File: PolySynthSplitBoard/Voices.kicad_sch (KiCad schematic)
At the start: 42 parts, among them J701 VoiceBoardConn_20P_200P, J702 VoiceBoardConn_20P_200P, J703 VoiceBoardConn_20P_200P, J704 VoiceBoardConn_20P_200P, J705 VoiceBoardConn_20P_200P, J706 VoiceBoardConn_20P_200P, U701 TCA9548APWR, U703 L7805, U704 L7905

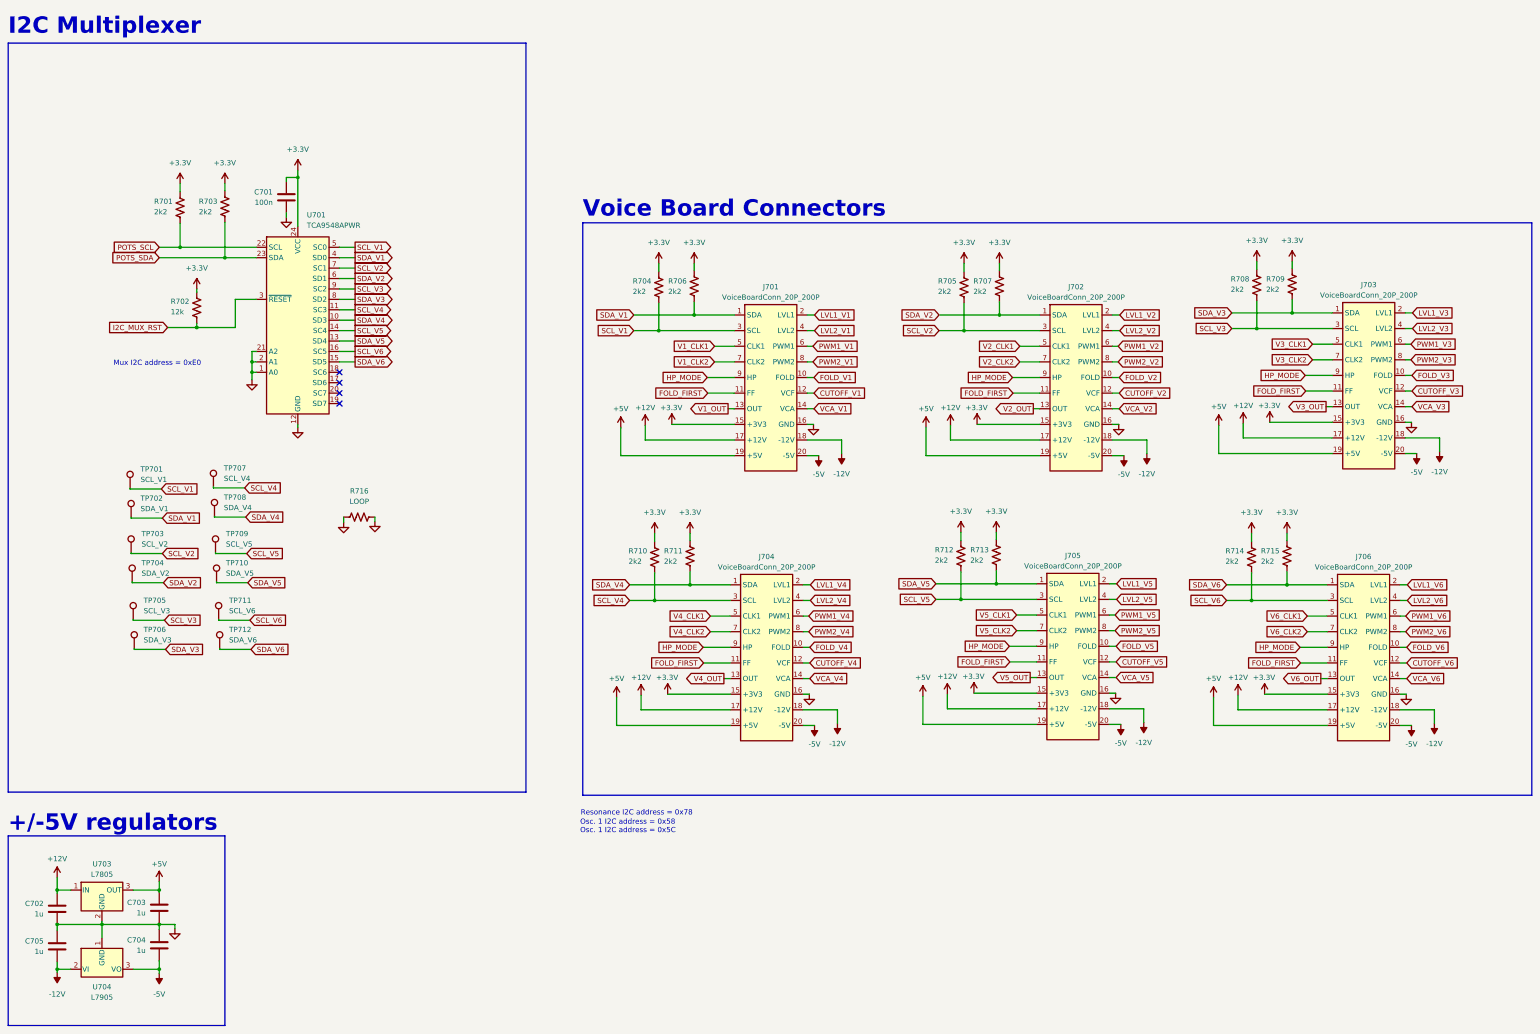
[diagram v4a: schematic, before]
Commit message: double buffering voice clock fixes
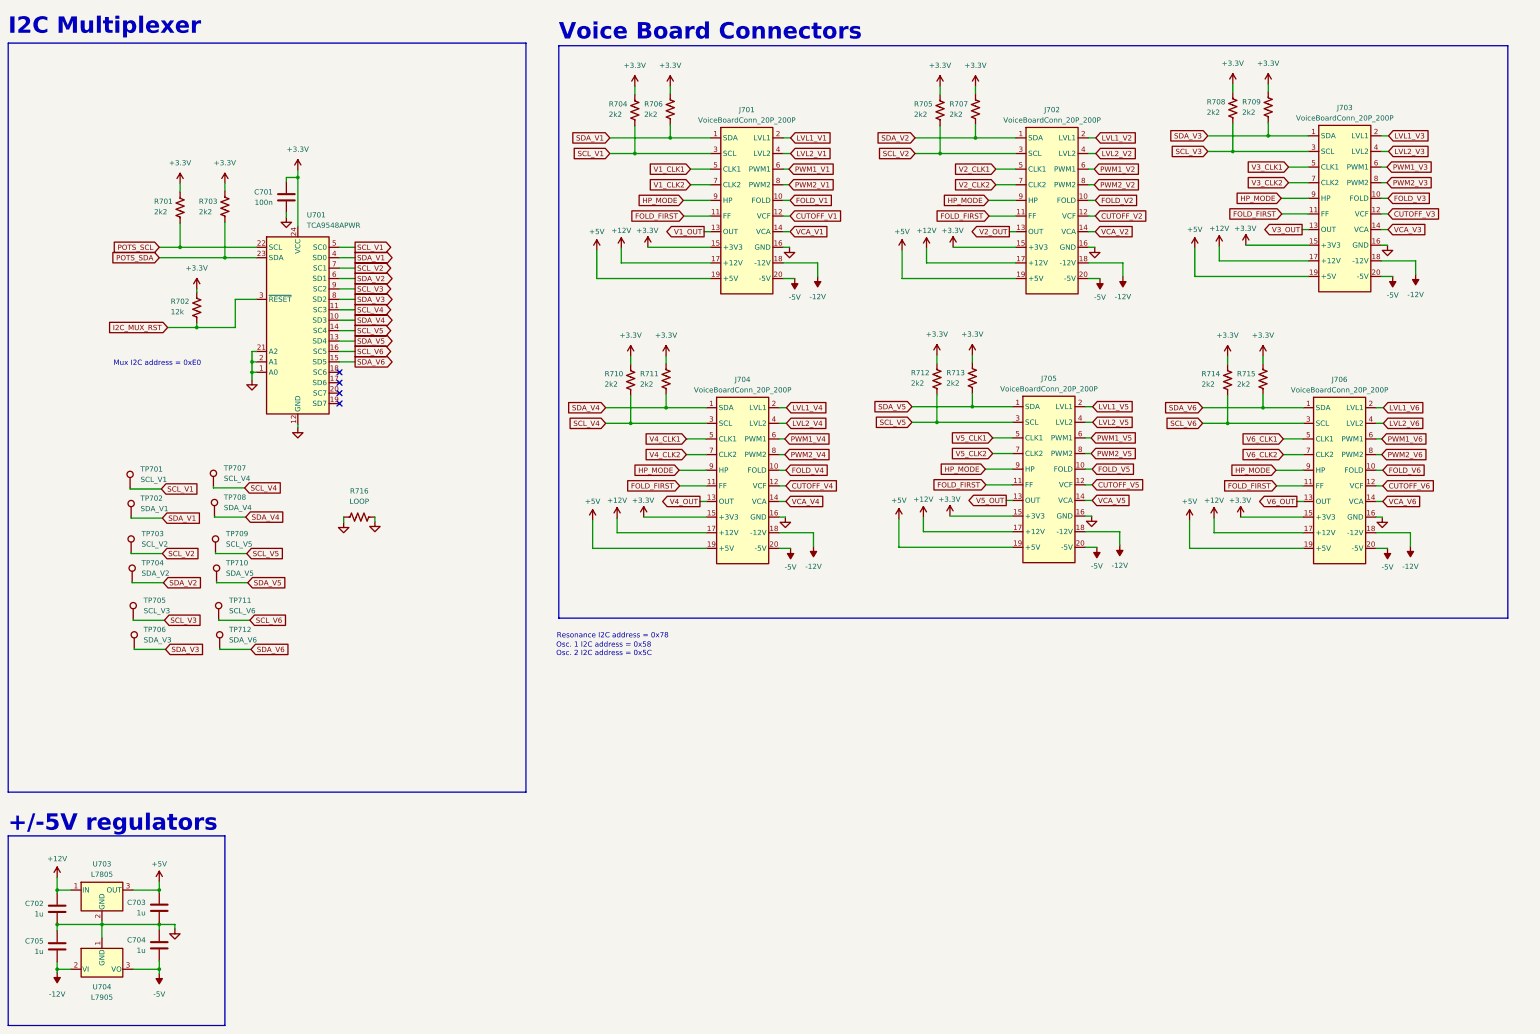
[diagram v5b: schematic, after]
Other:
- note added: "Osc. 1 I2C address = 0x58 Osc. 2 I2C address = 0x5C"
- note removed: "Osc. 1 I2C address = 0x58 Osc. 1 I2C address = 0x5C"
- moved on the sheet: J701, J702, J703, J704, J705, J706, R704, R705, R706, R707, R708, R709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
